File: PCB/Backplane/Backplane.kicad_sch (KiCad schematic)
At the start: 34 parts, among them J1 ICSP, SW1 Boot, U1 LM4040DBZ-3, U2 THVD1420D, U3 PIC18F25Q43, U4 TPS629210

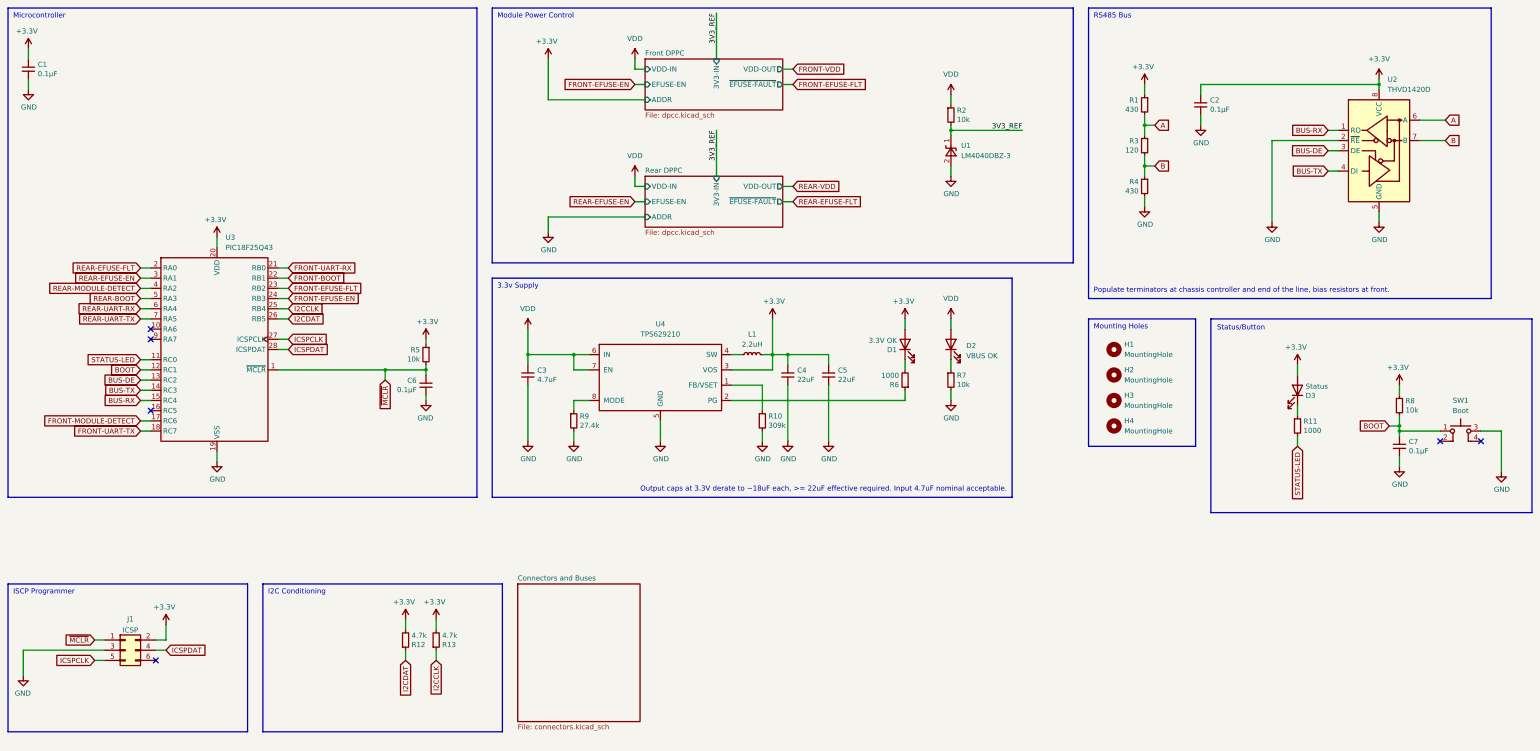
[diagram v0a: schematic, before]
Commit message: Add ESD protection to the RS485 networks.
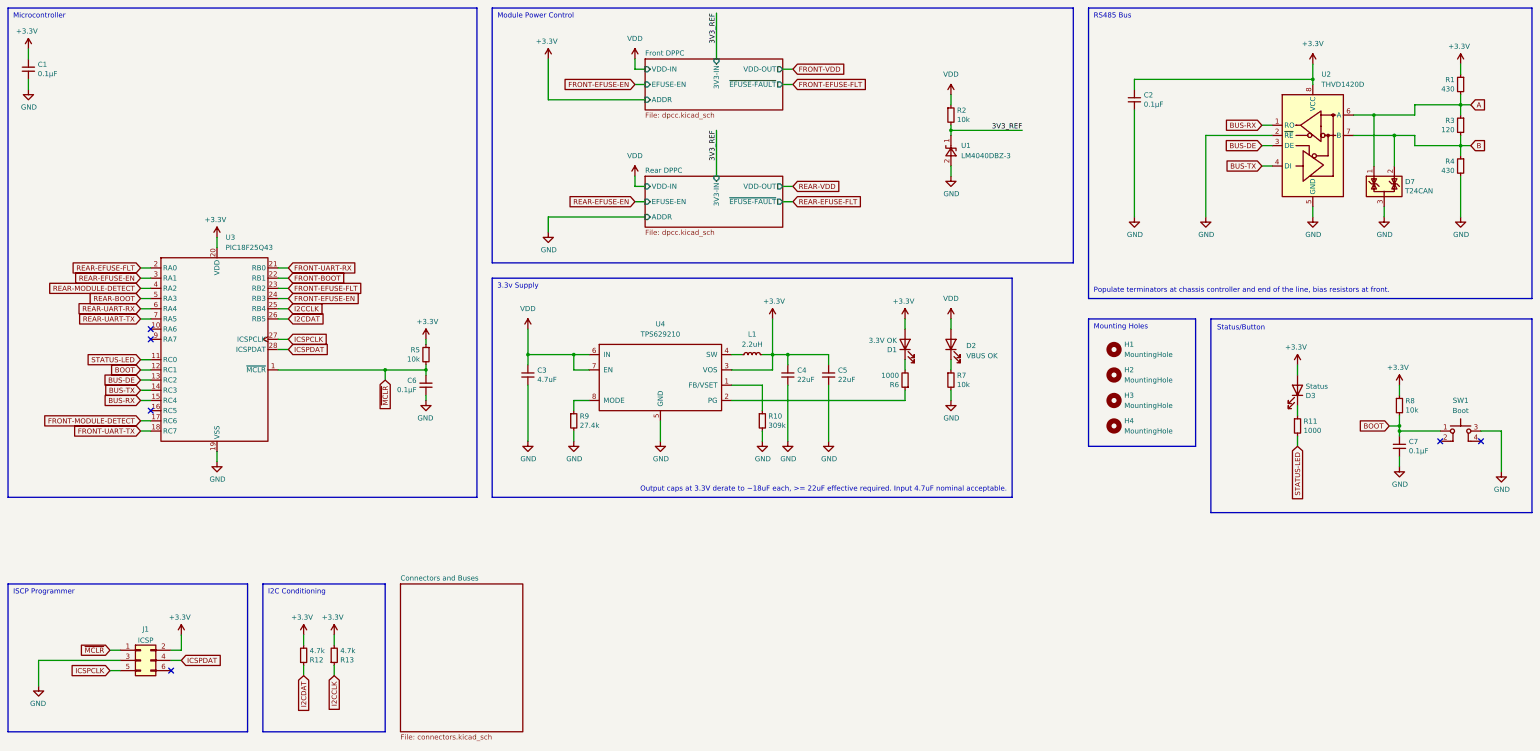
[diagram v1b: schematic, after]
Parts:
- added D7: T24CAN, Package_TO_SOT_SMD:SOT-23, symbol Power_Protection:NUP2105L
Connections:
- net A: now also D7.1 (K)
- net B: now also D7.2 (K)
- net GND: now also D7.3 (A)
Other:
- moved on the sheet: C2, J1, R1, R12, R13, R3, R4, U2

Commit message: Fix up power LEDs on regulators.
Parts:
- added D8: 3.3V OK, LED_SMD:LED_0603_1608Metric, symbol Device:LED
- added R31: 10k, Resistor_SMD:R_0603_1608Metric, symbol Device:R_Small
- D1: value 3.3V OK -> 3.3V Fault; DIGIKEY 3147-B19Y1UYG-20C000313U1930CT-ND -> 3147-B19Y1USD-20C000113U1930CT-ND
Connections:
- net +3.3V: now also D8.2 (A)
- net GND: now also R31.2
- new net: D8.1 (K), R31.1
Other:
- moved on the sheet: D2, R7

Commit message: Correct Digikey part numbers.
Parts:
- D7: DIGIKEY STOCK -> CDSOT23-T24CANCT-ND
- R31: value 10k -> 1000; DIGIKEY P10.0KHCT-ND -> P1.0KHCT-ND
- U1: DIGIKEY (none) -> 31-LM4040C33FTACT-ND
- U3: DIGIKEY STOCK -> 150-PIC18F25Q43-I/SS-ND
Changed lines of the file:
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@@
 			)
 		)
-		(property "Value" "10k"
+		(property "Value" "1000"
 			(at 250.4186 109.093 0)
 			(effects
@@
 			)
 		)
-		(property "DIGIKEY" "P10.0KHCT-ND"
+		(property "DIGIKEY" "P1.0KHCT-ND"
 			(at 248.92 107.95 0)
 			(effects
@@
 			)
 		)
-		(property "DIGIKEY" "STOCK"
+		(property "DIGIKEY" "150-PIC18F25Q43-I/SS-ND"
 			(at 67.31 100.33 0)
 			(effects
@@
 			)
 		)
-		(property "DIGIKEY" "STOCK"
+		(property "DIGIKEY" "CDSOT23-T24CANCT-ND"
 			(at 358.14 59.69 0)
 			(effects
@@
 			(effects
 				(font
+					(size 1.27 1.27)
+				)
+				(hide yes)
+			)
+		)
+		(property "DIGIKEY" "31-LM4040C33FTACT-ND"
+			(at 250.19 50.8 90)
+			(effects
+				(font

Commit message: feat: Upgrade backplane to a STM32G070KB.
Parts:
- removed U3: PIC18F25Q43, Package_SO:SSOP-28_5.3x10.2mm_P0.65mm, symbol KTANE:PIC18F25Q43
- added C25: 4.7uF, Capacitor_SMD:C_0603_1608Metric, symbol Device:C_Small
- added U11: STM32G070KBT6, Package_QFP:LQFP-32_7x7mm_P0.8mm, symbol KTANE:STM32G070KBTx
- H1, H2, H3, H4: footprint MountingHole:MountingHole_3.2mm_M3 -> KTANE:MountingHole_3.2mm_M3_NoCopper
- J1: value ICSP -> SWD
- R6: value 1000 -> 10k; DIGIKEY P1.00KHCT-ND -> P10.0KHCT-ND
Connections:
- net ICSPCLK is gone; now on net GND: J1.5 (Pin_5)
- net +3.3V: now also J1.1 (Pin_1), C25.1, U11.4 (VDD); no longer D1.2 (A), J1.2 (Pin_2)
- net BOOT: now also U11.11 (PA4)
- net BUS-DE: now also U11.16 (PB1)
- net BUS-RX: now also U11.15 (PB0)
- net BUS-TX: now also U11.12 (PA5)
- net FRONT-BOOT: now also U11.20 (PC6)
- net FRONT-EFUSE-EN: now also U11.23 (PA10/PA12)
- net FRONT-EFUSE-FLT: now also U11.22 (PA9/PA11)
- net FRONT-MODULE-DETECT: now also U11.18 (PA8)
- net FRONT-UART-RX: now also U11.21 (NC/PA10)
- net FRONT-UART-TX: now also U11.19 (NC/PA9)
- net GND: now also C25.2, U11.5 (VSS); no longer J1.3 (Pin_3)
- net I2CCLK: now also U11.30 (PB6)
- net I2CDAT: now also U11.31 (PB7)
- net REAR-BOOT: now also U11.9 (PA2)
- net REAR-EFUSE-EN: now also U11.2 (PC14)
- net REAR-EFUSE-FLT: now also U11.1 (PB9)
- net REAR-MODULE-DETECT: now also U11.3 (PC15)
- net REAR-UART-RX: now also U11.7 (PA0)
- net REAR-UART-TX: now also U11.8 (PA1)
- net STATUS-LED: now also U11.13 (PA6)
- net VDD: now also D1.2 (A)
- net ICSPDAT renamed SWCLK
- net SWCLK: now also U11.25 (PA14)
- net ~{MCLR} renamed ~{RESET}
- net ~{RESET}: now also J1.3 (Pin_3), U11.6 (NRST); no longer J1.1 (Pin_1)
- new net FRONT-ILM: U11.17 (PB2)
- new net REAR-ILM: U11.10 (PA3)
- new net SWDIO: J1.2 (Pin_2), U11.24 (PA13)
- no-connect marks 6 -> 9
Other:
- sheet Front DPPC ports: added ILM; removed none
- sheet Rear DPPC ports: added ILM; removed none
- note added: "Single Wire Debug"
- note removed: "ISCP Programmer"
- note removed: "Microcontroller"
- moved on the sheet: C1, C6, J1, R5
